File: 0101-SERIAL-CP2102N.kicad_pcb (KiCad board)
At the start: 4 copper layers, 19.6 x 35 mm, 42 parts, among them J1 USB-C, J2 Conn_02x04_Odd_Even, Q1 PUMH4,115, U1 CP2102N-A02-GQFN24

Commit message: Update package of USB-C
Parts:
- moved J1 2.60 mm to (106.6, 110.0)
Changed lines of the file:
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@@
   )
   (footprint "JLC-SMT:HRO_TYPE-C-31-M-12" locked (layer "F.Cu")
-    (at 104 110 -90)
+    (at 106.6 110 -90)
     (property "Datasheet" "https://www.usb.org/sites/default/files/documents/usb_type-c.zip")
     (property "Manufacturer" "HRO")
@@
       (effects (font (size 1 1) (thickness 0.15)))
     )
-    (fp_line (start 4.7 -1.9) (end 4.7 -0.3) (layer "F.SilkS") (width 0.12))
-    (fp_line (start -4.7 -1.9) (end -4.7 -0.3) (layer "F.SilkS") (width 0.12))
-    (fp_line (start -5.32 -5.27) (end -5.32 4.15) (layer "F.CrtYd") (width 0.05))
-    (fp_line (start -5.32 -5.27) (end 5.32 -5.27) (layer "F.CrtYd") (width 0.05))
-    (fp_line (start 5.32 -5.27) (end 5.32 4.15) (layer "F.CrtYd") (width 0.05))
-    (fp_line (start -5.32 4.15) (end 5.32 4.15) (layer "F.CrtYd") (width 0.05))
-    (fp_line (start -4.47 -3.65) (end 4.47 -3.65) (layer "F.Fab") (width 0.1))
-    (fp_line (start -4.47 3.65) (end 4.47 3.65) (layer "F.Fab") (width 0.1))
-    (fp_line (start 4.47 -3.65) (end 4.47 3.65) (layer "F.Fab") (width 0.1))
-    (fp_line (start -4.47 -3.65) (end -4.47 3.65) (layer "F.Fab") (width 0.1))
-    (pad "" np_thru_hole circle locked (at -2.9 -2.6 270) (size 0.65 0.65) (drill 0.65) (layers *.Cu *.Mask))
-    (pad "" np_thru_hole circle locked (at 2.9 -2.6 270) (size 0.65 0.65) (drill 0.65) (layers *.Cu *.Mask))
-    (pad "A1" smd rect locked (at -3.2 -4.045 270) (size 0.6 1.45) (layers "F.Cu" "F.Paste" "F.Mask")
+    (fp_line (start 4.7 0.7) (end 4.7 2.3) (layer "F.SilkS") (width 0.12))
+    (fp_line (start -4.7 0.7) (end -4.7 2.3) (layer "F.SilkS") (width 0.12))
+    (fp_line (start -6 5.79) (end 6 5.79) (layer "Dwgs.User") (width 0.12))
+    (fp_line (start -5.32 -2.67) (end 5.32 -2.67) (layer "F.CrtYd") (width 0.05))
+    (fp_line (start -5.32 6.75) (end 5.32 6.75) (layer "F.CrtYd") (width 0.05))
+    (fp_line (start 5.32 -2.67) (end 5.32 6.75) (layer "F.CrtYd") (width 0.05))
+    (fp_line (start -5.32 -2.67) (end -5.32 6.75) (layer "F.CrtYd") (width 0.05))
+    (fp_line (start -4.47 -1.05) (end -4.47 6.25) (layer "F.Fab") (width 0.1))
+    (fp_line (start -4.47 -1.05) (end 4.47 -1.05) (layer "F.Fab") (width 0.1))
+    (fp_line (start 4.47 -1.05) (end 4.47 6.25) (layer "F.Fab") (width 0.1))
+    (fp_line (start -4.47 6.25) (end 4.47 6.25) (layer "F.Fab") (width 0.1))
+    (pad "" np_thru_hole circle locked (at 2.9 0 270) (size 0.65 0.65) (drill 0.65) (layers F&B.Cu *.Mask))
+    (pad "" np_thru_hole circle locked (at -2.9 0 270) (size 0.65 0.65) (drill 0.65) (layers F&B.Cu *.Mask))
+    (pad "A1" smd rect locked (at -3.2 -1.445 270) (size 0.6 1.45) (layers "F.Cu" "F.Paste" "F.Mask")
       (net 2 "GND") (pinfunction "GND") (pintype "passive"))
-    (pad "A4" smd rect locked (at -2.4 -4.045 270) (size 0.6 1.45) (layers "F.Cu" "F.Paste" "F.Mask")
+    (pad "A4" smd rect locked (at -2.4 -1.445 270) (size 0.6 1.45) (layers "F.Cu" "F.Paste" "F.Mask")
       (net 3 "VBUS") (pinfunction "VBUS") (pintype "passive"))
-    (pad "A5" smd rect locked (at -1.25 -4.045 270) (size 0.3 1.45) (layers "F.Cu" "F.Paste" "F.Mask")
+    (pad "A5" smd rect locked (at -1.25 -1.445 270) (size 0.3 1.45) (layers "F.Cu" "F.Paste" "F.Mask")
       (net 10 "Net-(J1-PadA5)") (pinfunction "CC1") (pintype "bidirectional"))
-    (pad "A6" smd rect locked (at -0.25 -4.045 270) (size 0.3 1.45) (layers "F.Cu" "F.Paste" "F.Mask")
+    (pad "A6" smd rect locked (at -0.25 -1.445 270) (size 0.3 1.45) (layers "F.Cu" "F.Paste" "F.Mask")
       (net 12 "/D+") (pinfunction "D+") (pintype "bidirectional"))
-    (pad "A7" smd rect locked (at 0.25 -4.045 270) (size 0.3 1.45) (layers "F.Cu" "F.Paste" "F.Mask")
+    (pad "A7" smd rect locked (at 0.25 -1.445 270) (size 0.3 1.45) (layers "F.Cu" "F.Paste" "F.Mask")
       (net 11 "/D-") (pinfunction "D-") (pintype "bidirectional"))
-    (pad "A8" smd rect locked (at 1.25 -4.045 270) (size 0.3 1.45) (layers "F.Cu" "F.Paste" "F.Mask")
+    (pad "A8" smd rect locked (at 1.25 -1.445 270) (size 0.3 1.45) (layers "F.Cu" "F.Paste" "F.Mask")
       (net 13 "unconnected-(J1-PadA8)") (pinfunction "SBU1") (pintype "bidirectional+no_connect"))
-    (pad "A9" smd rect locked (at 2.4 -4.045 270) (size 0.6 1.45) (layers "F.Cu" "F.Paste" "F.Mask")
+    (pad "A9" smd rect locked (at 2.4 -1.445 270) (size 0.6 1.45) (layers "F.Cu" "F.Paste" "F.Mask")
       (net 3 "VBUS") (pinfunction "VBUS") (pintype "passive"))
-    (pad "A12" smd rect locked (at 3.2 -4.045 270) (size 0.6 1.45) (layers "F.Cu" "F.Paste" "F.Mask")
+    (pad "A12" smd rect locked (at 3.2 -1.445 270) (size 0.6 1.45) (layers "F.Cu" "F.Paste" "F.Mask")
       (net 2 "GND") (pinfunction "GND") (pintype "passive"))
-    (pad "B1" smd rect locked (at 3.2 -4.045 270) (size 0.6 1.45) (layers "F.Cu" "F.Paste" "F.Mask")
+    (pad "B1" smd rect locked (at 3.2 -1.445 270) (size 0.6 1.45) (layers "F.Cu" "F.Paste" "F.Mask")
       (net 2 "GND") (pinfunction "GND") (pintype "passive"))
-    (pad "B4" smd rect locked (at 2.4 -4.045 270) (size 0.6 1.45) (layers "F.Cu" "F.Paste" "F.Mask")
+    (pad "B4" smd rect locked (at 2.4 -1.445 270) (size 0.6 1.45) (layers "F.Cu" "F.Paste" "F.Mask")
       (net 3 "VBUS") (pinfunction "VBUS") (pintype "passive"))
-    (pad "B5" smd rect locked (at 1.75 -4.045 270) (size 0.3 1.45) (layers "F.Cu" "F.Paste" "F.Mask")
+    (pad "B5" smd rect locked (at 1.75 -1.445 270) (size 0.3 1.45) (layers "F.Cu" "F.Paste" "F.Mask")
       (net 14 "Net-(J1-PadB5)") (pinfunction "CC2") (pintype "bidirectional"))
-    (pad "B6" smd rect locked (at 0.75 -4.045 270) (size 0.3 1.45) (layers "F.Cu" "F.Paste" "F.Mask")
+    (pad "B6" smd rect locked (at 0.75 -1.445 270) (size 0.3 1.45) (layers "F.Cu" "F.Paste" "F.Mask")
       (net 12 "/D+") (pinfunction "D+") (pintype "bidirectional"))
-    (pad "B7" smd rect locked (at -0.75 -4.045 270) (size 0.3 1.45) (layers "F.Cu" "F.Paste" "F.Mask")
+    (pad "B7" smd rect locked (at -0.75 -1.445 270) (size 0.3 1.45) (layers "F.Cu" "F.Paste" "F.Mask")
       (net 11 "/D-") (pinfunction "D-") (pintype "bidirectional"))
-    (pad "B8" smd rect locked (at -1.75 -4.045 270) (size 0.3 1.45) (layers "F.Cu" "F.Paste" "F.Mask")
+    (pad "B8" smd rect locked (at -1.75 -1.445 270) (size 0.3 1.45) (layers "F.Cu" "F.Paste" "F.Mask")
       (net 9 "unconnected-(J1-PadB8)") (pinfunction "SBU2") (pintype "bidirectional+no_connect"))
-    (pad "B9" smd rect locked (at -2.4 -4.045 270) (size 0.6 1.45) (layers "F.Cu" "F.Paste" "F.Mask")
+    (pad "B9" smd rect locked (at -2.4 -1.445 270) (size 0.6 1.45) (layers "F.Cu" "F.Paste" "F.Mask")
       (net 3 "VBUS") (pinfunction "VBUS") (pintype "passive"))
-    (pad "B12" smd rect locked (at -3.2 -4.045 270) (size 0.6 1.45) (layers "F.Cu" "F.Paste" "F.Mask")
+    (pad "B12" smd rect locked (at -3.2 -1.445 270) (size 0.6 1.45) (layers "F.Cu" "F.Paste" "F.Mask")
       (net 2 "GND") (pinfunction "GND") (pintype "passive"))
-    (pad "S1" thru_hole roundrect locked (at 4.325 1.05 270) (size 1.4 2) (drill oval 0.6 1.2 (offset 0.2 -0.2)) (layers *.Cu *.Mask) (roundrect_rratio 0.25)
+    (pad "S1" thru_hole roundrect locked (at 4.325 -0.53 270) (size 1.4 2.1) (drill oval 0.6 1.7 (offset 0.2 0)) (layers *.Cu *.Mask) (roundrect_rratio 0.25)
       (net 2 "GND") (pinfunction "SHIELD") (pintype "passive"))
-    (pad "S1" thru_hole roundrect locked (at -4.325 -3.13 270) (size 1.4 2.1) (drill oval 0.6 1.7 (offset -0.2 0)) (layers *.Cu *.Mask) (roundrect_rratio 0.25)
+    (pad "S1" thru_hole roundrect locked (at -4.325 3.65 270) (size 1.4 2) (drill oval 0.6 1.2 (offset -0.2 -0.2)) (layers *.Cu *.Mask) (roundrect_rratio 0.25)
       (net 2 "GND") (pinfunction "SHIELD") (pintype "passive"))
-    (pad "S1" thru_hole roundrect locked (at 4.325 -3.13 270) (size 1.4 2.1) (drill oval 0.6 1.7 (offset 0.2 0)) (layers *.Cu *.Mask) (roundrect_rratio 0.25)
+    (pad "S1" thru_hole roundrect locked (at 4.325 3.65 270) (size 1.4 2) (drill oval 0.6 1.2 (offset 0.2 -0.2)) (layers *.Cu *.Mask) (roundrect_rratio 0.25)
       (net 2 "GND") (pinfunction "SHIELD") (pintype "passive"))
-    (pad "S1" thru_hole roundrect locked (at -4.325 1.05 270) (size 1.4 2) (drill oval 0.6 1.2 (offset -0.2 -0.2)) (layers *.Cu *.Mask) (roundrect_rratio 0.25)
+    (pad "S1" thru_hole roundrect locked (at -4.325 -0.53 270) (size 1.4 2.1) (drill oval 0.6 1.7 (offset -0.2 0)) (layers *.Cu *.Mask) (roundrect_rratio 0.25)
       (net 2 "GND") (pinfunction "SHIELD") (pintype "passive"))
     (model "${CUSTOM_DIR}/HRO_TYPE-C-31-M-12.step"
-      (offset (xyz -4.45 -3.65 0))
+      (offset (xyz -4.45 -6.25 0))
       (scale (xyz 1 1 1))
       (rotate (xyz 0 0 0))

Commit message: Tune power tracks
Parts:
- moved R12 0.20 mm to (116.0, 117.7)
- moved R13 0.20 mm to (112.0, 117.7)
- moved R14 0.20 mm to (112.0, 102.3)
- moved R15 0.20 mm to (116.0, 102.3)
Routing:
- net VDD: track 44.9 -> 7.58 mm
- net Net-(R3-Pad2): track 13.9 -> 10.7 mm
- net /RTS/BOOT: track 38.7 -> 39.6 mm
- net GND: vias 30 -> 35
- removed copper zone on In1.Cu, net GND
- removed copper zone on In1.Cu, net VBUS

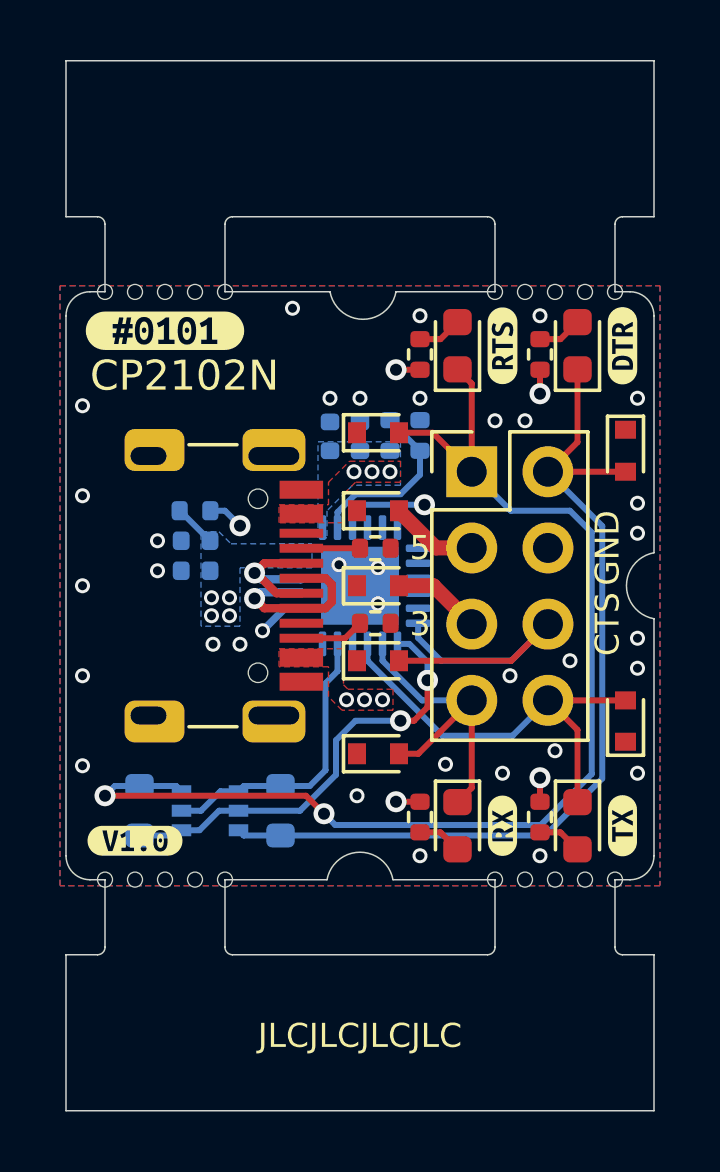
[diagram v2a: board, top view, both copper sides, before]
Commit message: Move CC 5.1K pull-down resistors to B.Cu
* so that they can be soldered together with CP2102N
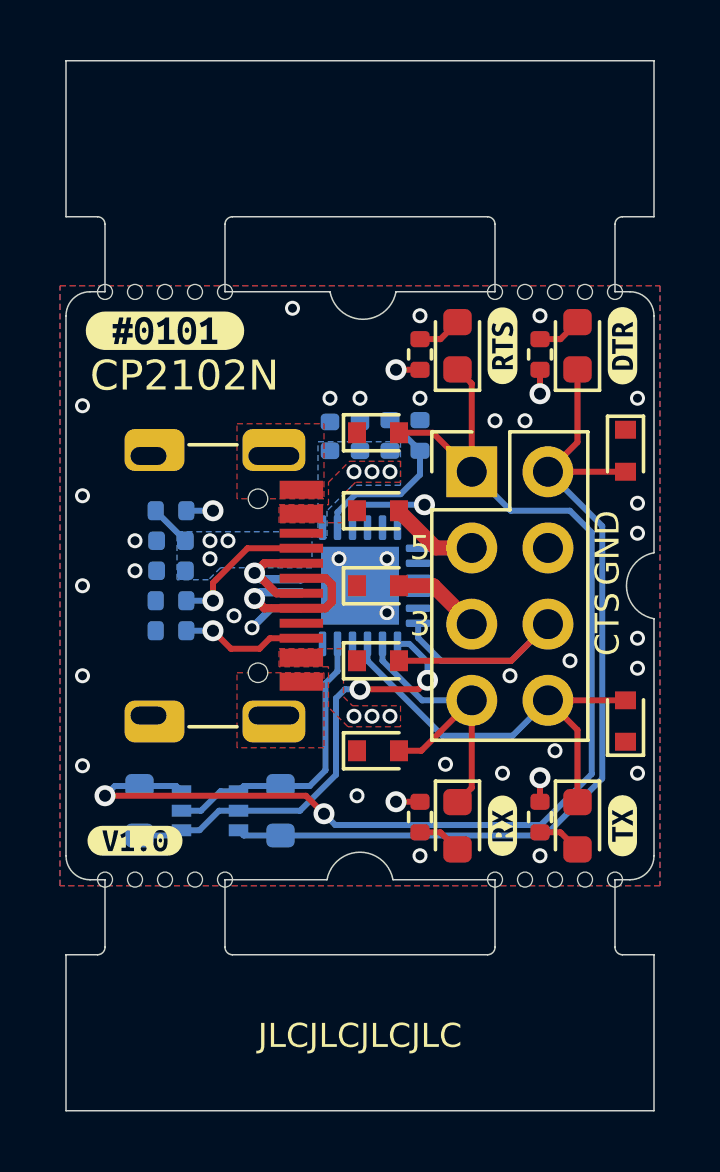
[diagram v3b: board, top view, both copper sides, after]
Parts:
- R4, R5: moved to B.Cu
- moved R4 7.03 mm to (103.7, 110.5), turned to 180 degrees
- moved R5 6.81 mm to (103.7, 111.5), turned to 180 degrees
- moved C1 0.82 mm to (103.7, 108.5)
- moved C3 0.82 mm to (103.7, 109.5)
- moved R3 0.80 mm to (103.7, 107.5)
- moved D8 0.10 mm to (110.6, 115.5)
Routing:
- net Net-(J1-PadA5): track 1.95 -> 4.91 mm, vias 0 -> 1
- net Net-(J1-PadB5): track 2.16 -> 4.23 mm, vias 0 -> 1
- net Net-(R3-Pad2): track 10.7 -> 11.3 mm
- net GND: track 3.87 -> 4.18 mm, vias 35 -> 34
- net VDD: track 7.58 -> 7.57 mm, vias 8 -> 7

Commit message: Make silks better
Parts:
- removed kibuzzard-63351A9D: G***, kibuzzard-63351A9D
- added kibuzzard-6344EE61: G***, kibuzzard-6344EE61, F.Cu at (118.2, 111.3)
- added kibuzzard-6344EE6E: G***, kibuzzard-6344EE6E, F.Cu at (118.2, 108.7)
- added kibuzzard-6344EEF9: G***, kibuzzard-6344EEF9, F.Cu at (111.6, 108.7)
- added kibuzzard-6344EF12: G***, kibuzzard-6344EF12, F.Cu at (111.6, 111.3)
- added kibuzzard-6344F0D2: G***, kibuzzard-6344F0D2, F.Cu at (102.5, 118.5)
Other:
- board text removed: "3"
- board text removed: "5"
- board text removed: "CTS"
- board text removed: "GND"

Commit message: Fix outline
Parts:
- removed kibuzzard-6344F0D2: G***, kibuzzard-6344F0D2
- added kibuzzard-6346685F: G***, kibuzzard-6346685F, F.Cu at (102.5, 118.5)
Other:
- outline, holes or cut-outs redrawn
